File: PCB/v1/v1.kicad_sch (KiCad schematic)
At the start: 80 parts, among them J1 Screw_Terminal_01x02, Q2 BC548, SW1 Push Button, SW2 Push Button, U1 4060, U10 7400, U2 4060, U3 CD4026BE, U4 CD4026BE, U5 CD4026BE, U6 CD4026BE, U7 CD4026BE, U8 CD4026BE, Y1 32.768kHz

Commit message: Updated Schematic
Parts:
- added C10, C2, C3, C4, C5, C6, C7, C8, C9: 0.1u, Capacitor_SMD:C_0805_2012Metric_Pad1.18x1.45mm_HandSolder, symbol Device:C
- U10: footprint Package_DIP:SMDIP-14_W7.62mm -> Package_DIP:DIP-14_W10.16mm
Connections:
- net +6V: now also C10.1, C2.1, C3.1, C4.1, C5.1, C6.1, C7.1, C8.1, C9.1
- net GND: now also C10.2, C2.2, C3.2, C4.2, C5.2, C6.2, C7.2, C8.2, C9.2
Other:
- moved on the sheet: R51

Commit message: PCB routed V5
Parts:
- C1: footprint Capacitor_SMD:C_0805_2012Metric -> Capacitor_SMD:C_0805_2012Metric_Pad1.18x1.45mm_HandSolder
- D1: footprint LED_SMD:LED_0805_2012Metric -> LED_SMD:LED_0805_2012Metric_Pad1.15x1.40mm_HandSolder
- R1, R10, R11, R12, R13, R14, R15, R16, R17, R18, R19, R2, R20, R21, R22, R23, R24, R25, R26, R27, R28, R29, R3, R30, R31, R32, R33, R34, R35, R36, R37, R38, R39, R4, R40, R41, R42, R43, R44, R45, R46, R47, R48, R49, R5, R50, R51, R52, R6, R7, R8, R9: footprint Resistor_SMD:R_0805_2012Metric -> Resistor_SMD:R_0805_2012Metric_Pad1.20x1.40mm_HandSolder
- U1, U2: footprint Package_SO:SOIC-16_3.9x9.9mm_P1.27mm -> Package_DIP:DIP-16_W7.62mm_LongPads
- U10: footprint Package_DIP:DIP-14_W10.16mm -> Package_DIP:DIP-14_W7.62mm_LongPads
- U3, U4, U5, U6, U7, U8: footprint Package_DIP:DIP-16_W7.62mm -> Package_DIP:DIP-16_W7.62mm_LongPads

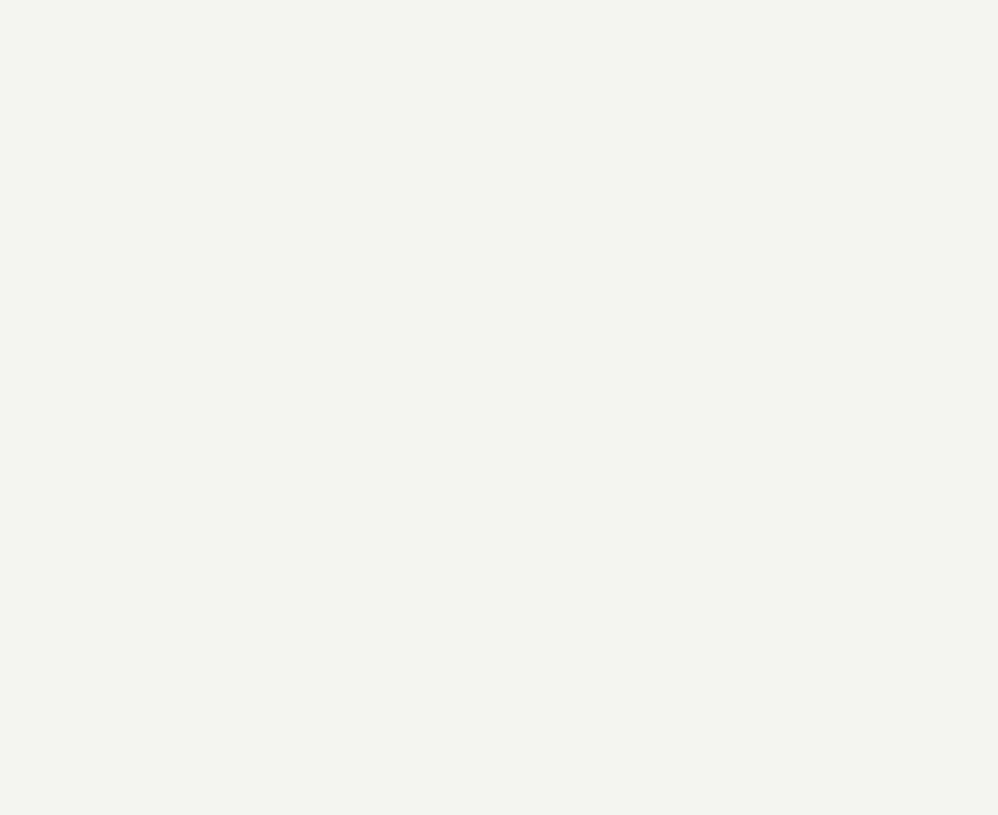
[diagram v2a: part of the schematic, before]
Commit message: Added Mounted Holes and Logos
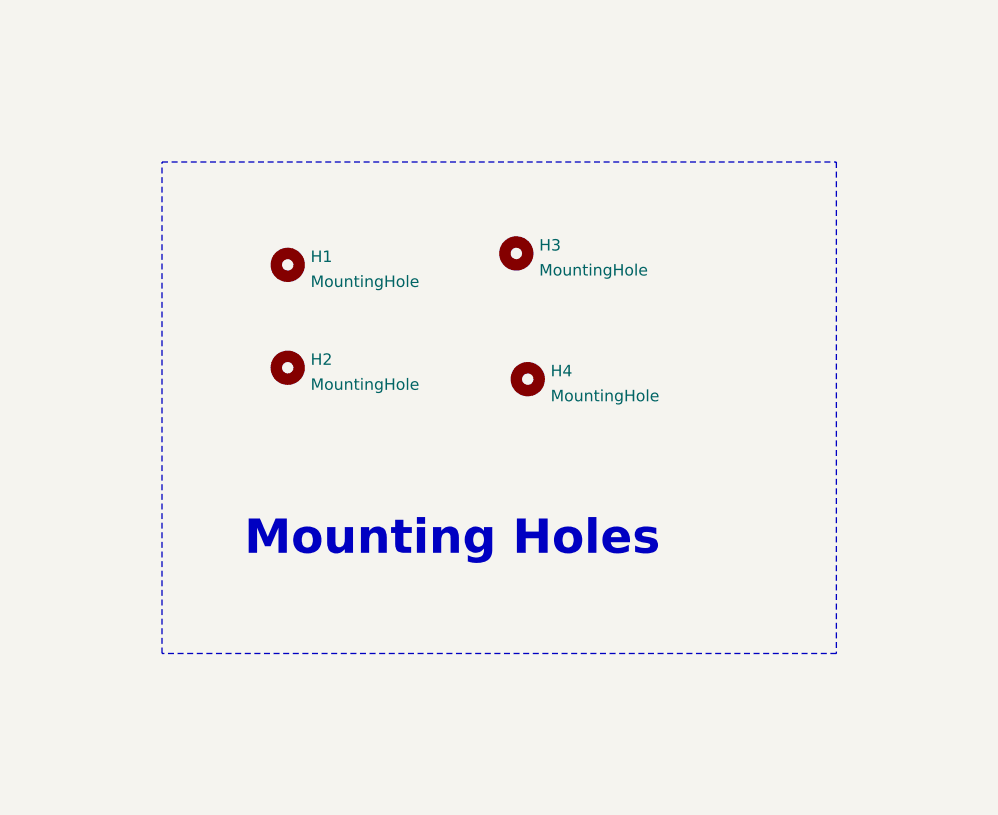
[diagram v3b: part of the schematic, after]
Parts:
- added H1, H2, H3, H4: MountingHole, MountingHole:MountingHole_3.2mm_M3, symbol Mechanical:MountingHole
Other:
- note added: "Mounting Holes"
